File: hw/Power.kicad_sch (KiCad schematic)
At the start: 3 parts, among them Q17 SK2301AAT, SW4 SW_SPDT

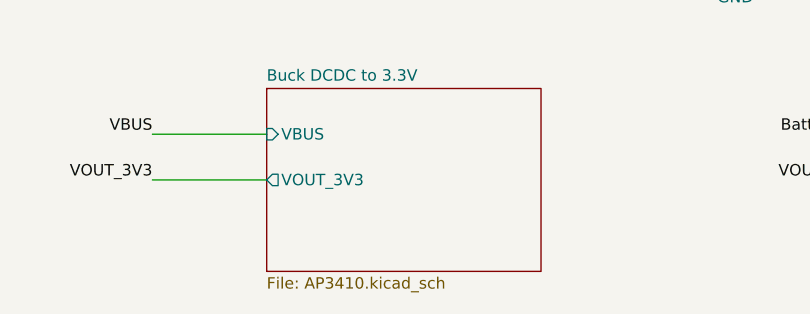
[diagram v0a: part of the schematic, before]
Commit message: replace AP3410 to SY8088IAAC
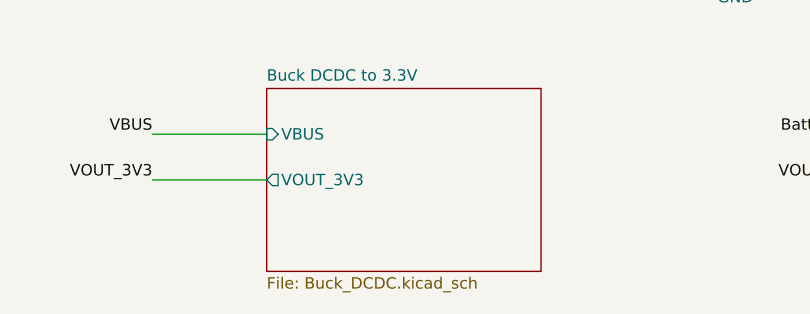
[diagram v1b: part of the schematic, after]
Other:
- sheet Buck DCDC to 3.3V: file AP3410.kicad_sch -> Buck_DCDC.kicad_sch
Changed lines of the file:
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@@
       (effects (font (size 1.27 1.27)) (justify left bottom))
     )
-    (property "Sheetfile" "AP3410.kicad_sch" (at 91.44 86.9446 0)
+    (property "Sheetfile" "Buck_DCDC.kicad_sch" (at 91.44 86.9446 0)
       (effects (font (size 1.27 1.27)) (justify left top))
     )

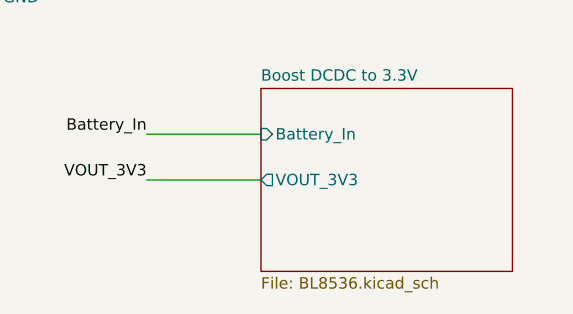
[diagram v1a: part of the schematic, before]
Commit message: replace BL8536 with ME2118C33M5G in schematic
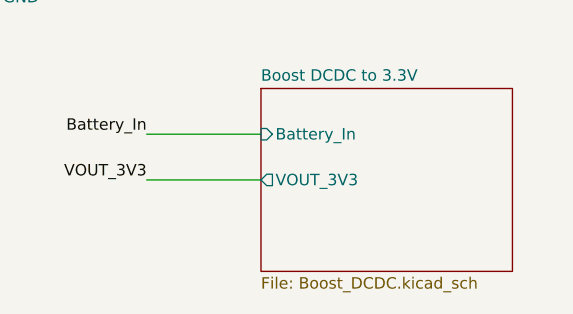
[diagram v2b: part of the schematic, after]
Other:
- sheet Boost DCDC to 3.3V: file BL8536.kicad_sch -> Boost_DCDC.kicad_sch
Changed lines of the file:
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@@
       (effects (font (size 1.27 1.27)) (justify left bottom))
     )
-    (property "Sheetfile" "BL8536.kicad_sch" (at 170.18 86.9446 0)
+    (property "Sheetfile" "Boost_DCDC.kicad_sch" (at 170.18 86.9446 0)
       (effects (font (size 1.27 1.27)) (justify left top))
     )

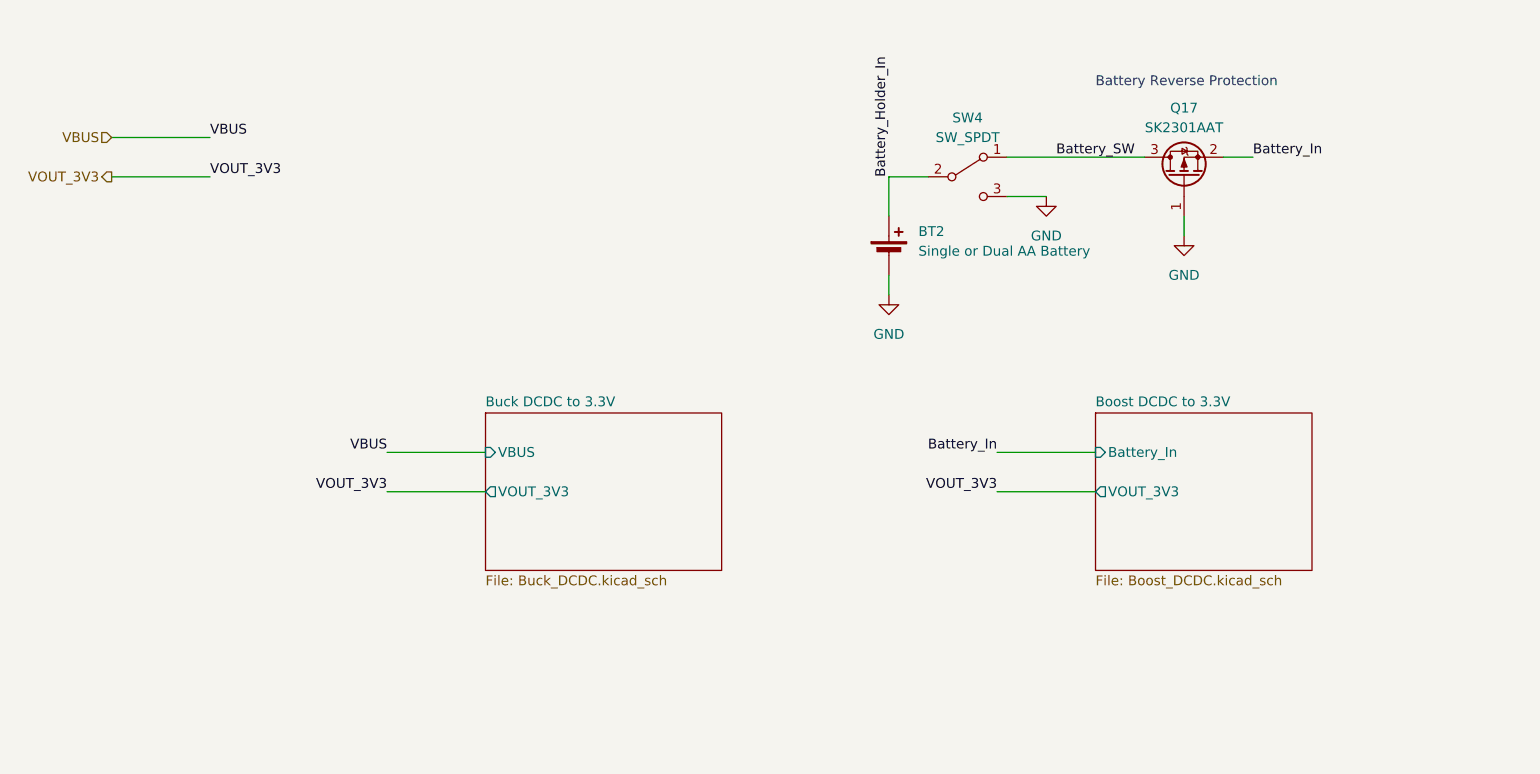
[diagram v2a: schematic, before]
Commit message: changed to use N-MOS as Reverse Battery Protection Circuits
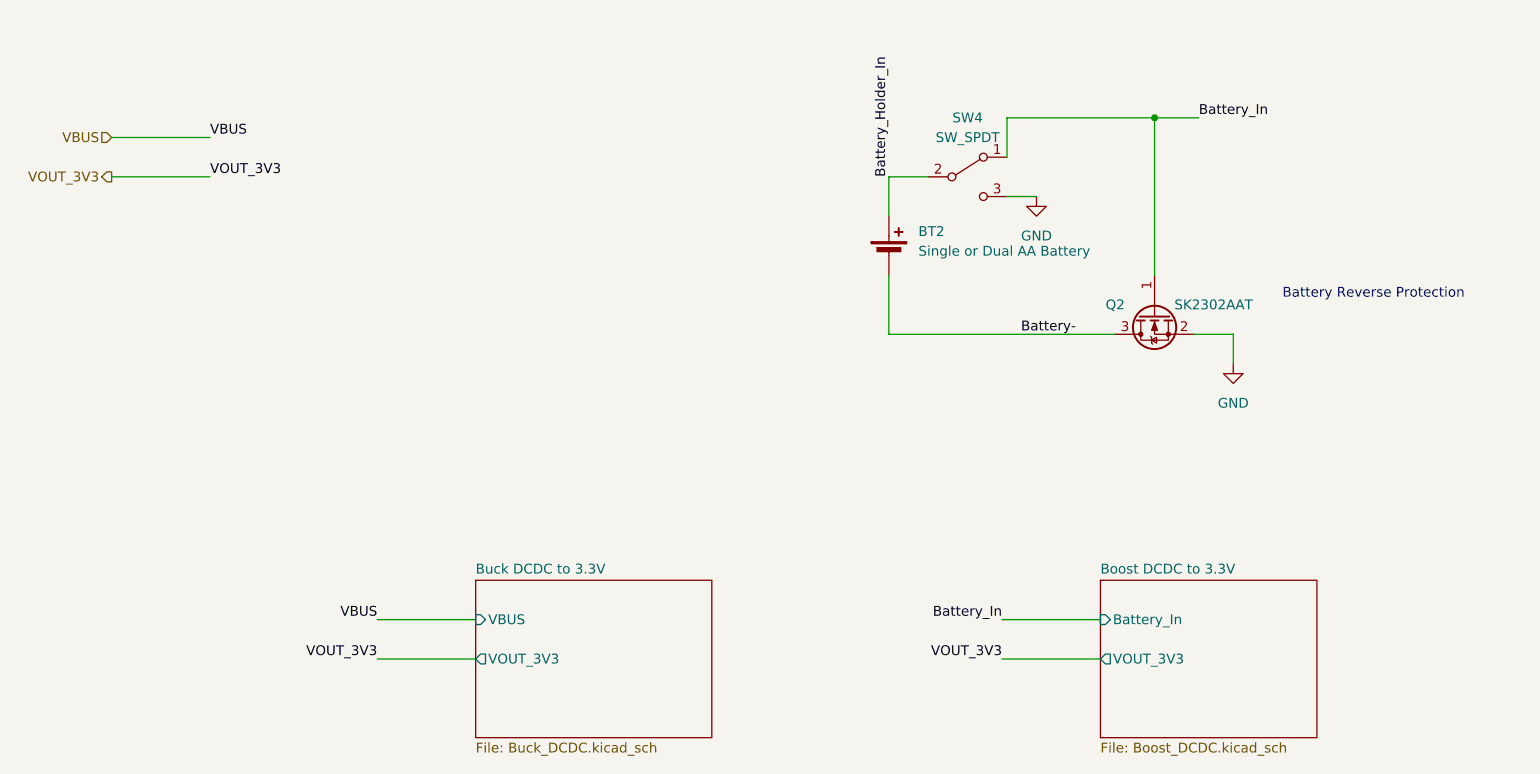
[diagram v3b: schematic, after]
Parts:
- removed Q17: SK2301AAT, Package_TO_SOT_SMD:SOT-523, symbol Device:Q_PMOS_GSD
- added Q2: SK2302AAT, Package_TO_SOT_SMD:SOT-523, symbol Device:Q_NMOS_GSD
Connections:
- net Battery_SW is gone; now on net Battery_In: SW4.1 (A)
- net Battery_In: now also Q2.1 (G)
- net GND: now also Q2.2 (S); no longer BT2.2 (-)
- new net Battery-: BT2.2 (-), Q2.3 (D)

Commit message: updated Sheet and Board Information
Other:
- company: Qingdao IotPi Information Technology Ltd., -> Beijing Exponential Deep Space
- title: KiCad 2023 Shen Zhen Badge -> KiCad 2023 Asia Badge
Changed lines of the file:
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@@
   (paper "A4")
   (title_block
-    (title "KiCad 2023 Shen Zhen Badge")
-    (date "2023-10-04")
+    (title "KiCad 2023 Asia Badge")
+    (date "2023-10-07")
     (rev "2")
-    (company "Qingdao IotPi Information Technology Ltd.,")
+    (company "Beijing Exponential Deep Space")
     (comment 1 "Designed by Yang Hongbo")
   )

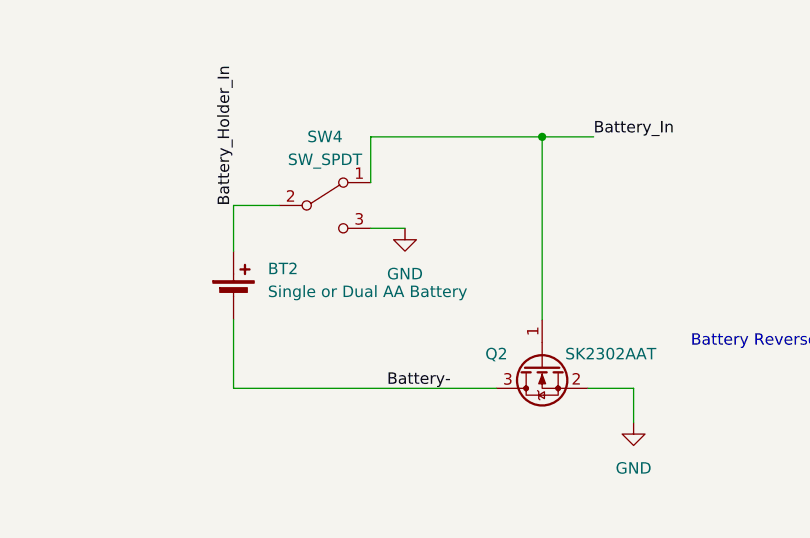
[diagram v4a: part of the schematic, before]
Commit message: fix SW4 pin3 to NC
was shorted to Battery+ when switch "OFF"
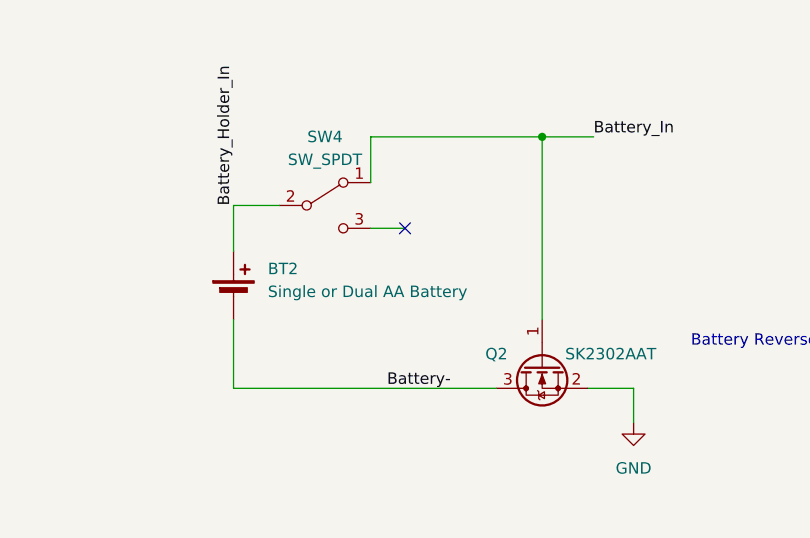
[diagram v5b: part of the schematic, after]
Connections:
- net GND: no longer SW4.3 (C)
- no-connect marks 0 -> 1
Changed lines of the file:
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@@
   (junction (at 177.8 27.94) (diameter 0) (color 0 0 0 0)
   )
+  (no_connect (at 162.56 38.1))
   (wire (pts (xy 158.75 38.1) (xy 162.56 38.1))
     (stroke (width 0) (type default))
@@
         )
       )
-    )
-  )
-  (symbol (lib_id "power:GND") (at 162.56 38.1 0) (unit 1)
-    (in_bom yes) (on_board yes) (dnp no) (fields_autoplaced)
-    (property "Reference" "#PWR09" (at 162.56 44.45 0)
-      (effects (font (size 1.27 1.27)) hide)
-    )
-    (property "Value" "GND" (at 162.56 43.18 0)
-      (effects (font (size 1.27 1.27)))
-    )
-    (property "Footprint" "" (at 162.56 38.1 0)
-      (effects (font (size 1.27 1.27)) hide)
-    )
-    (property "Datasheet" "" (at 162.56 38.1 0)
-      (effects (font (size 1.27 1.27)) hide)
-    )
-    (pin "1")
-    (instances
-      (project "KiConSZ2023"
-        (path "/8659c260-f029-4e72-8b9a-85fff45eea40/f453823a-a381-482a-9343-94fafcdcaf18"
-          (reference "#PWR09") (unit 1)
-        )
-      )
